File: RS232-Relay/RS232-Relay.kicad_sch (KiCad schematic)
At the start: 10 parts, among them J1 Conn_01x02, J2 Conn_01x02, K3 Relay_DPDT, Q1 2N3904, U2 4N25

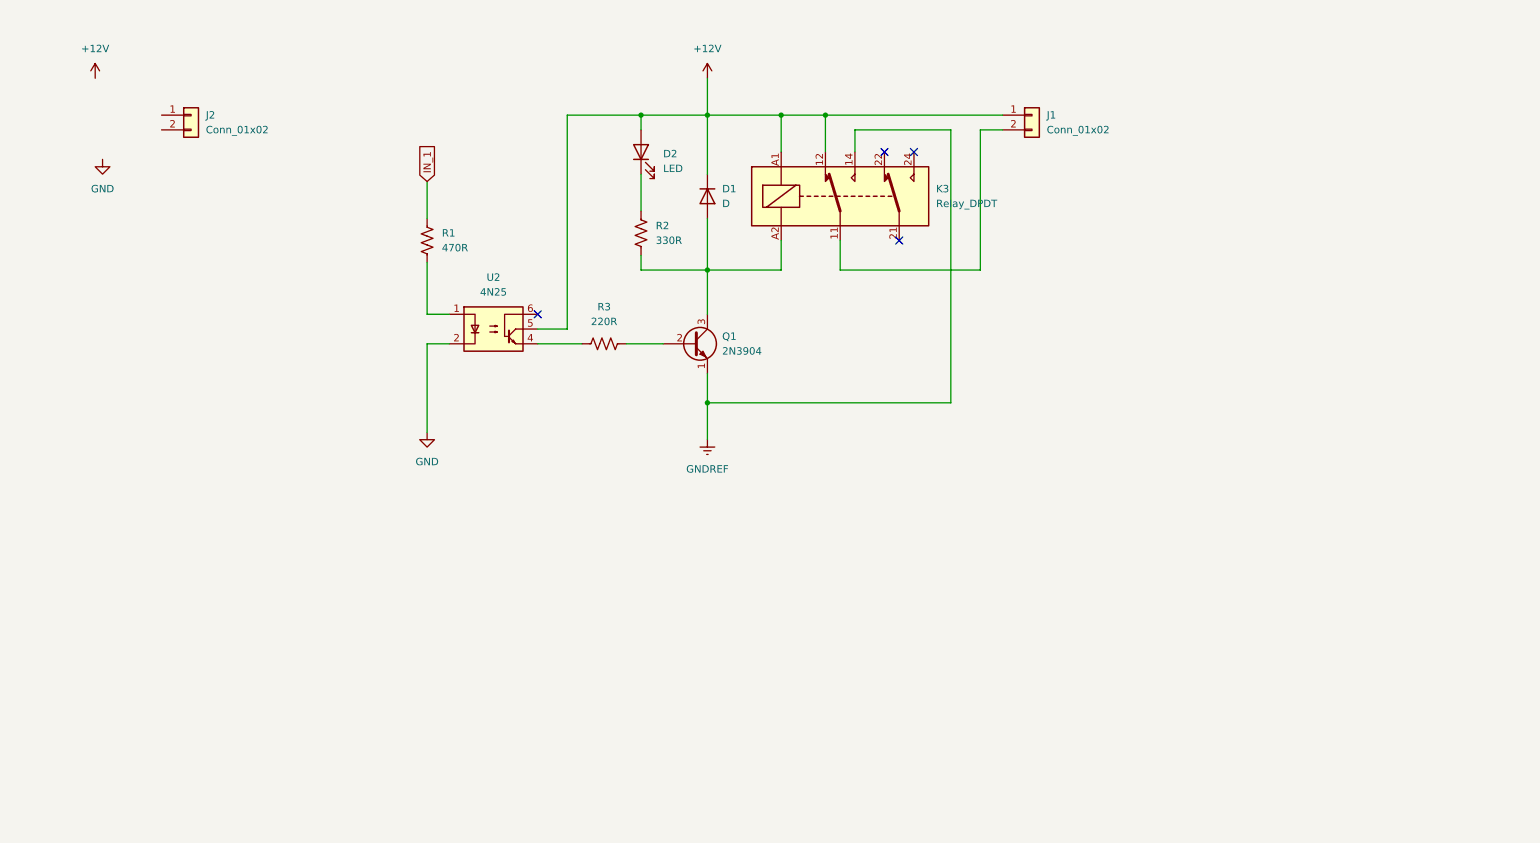
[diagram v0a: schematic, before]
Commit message: Relay layout
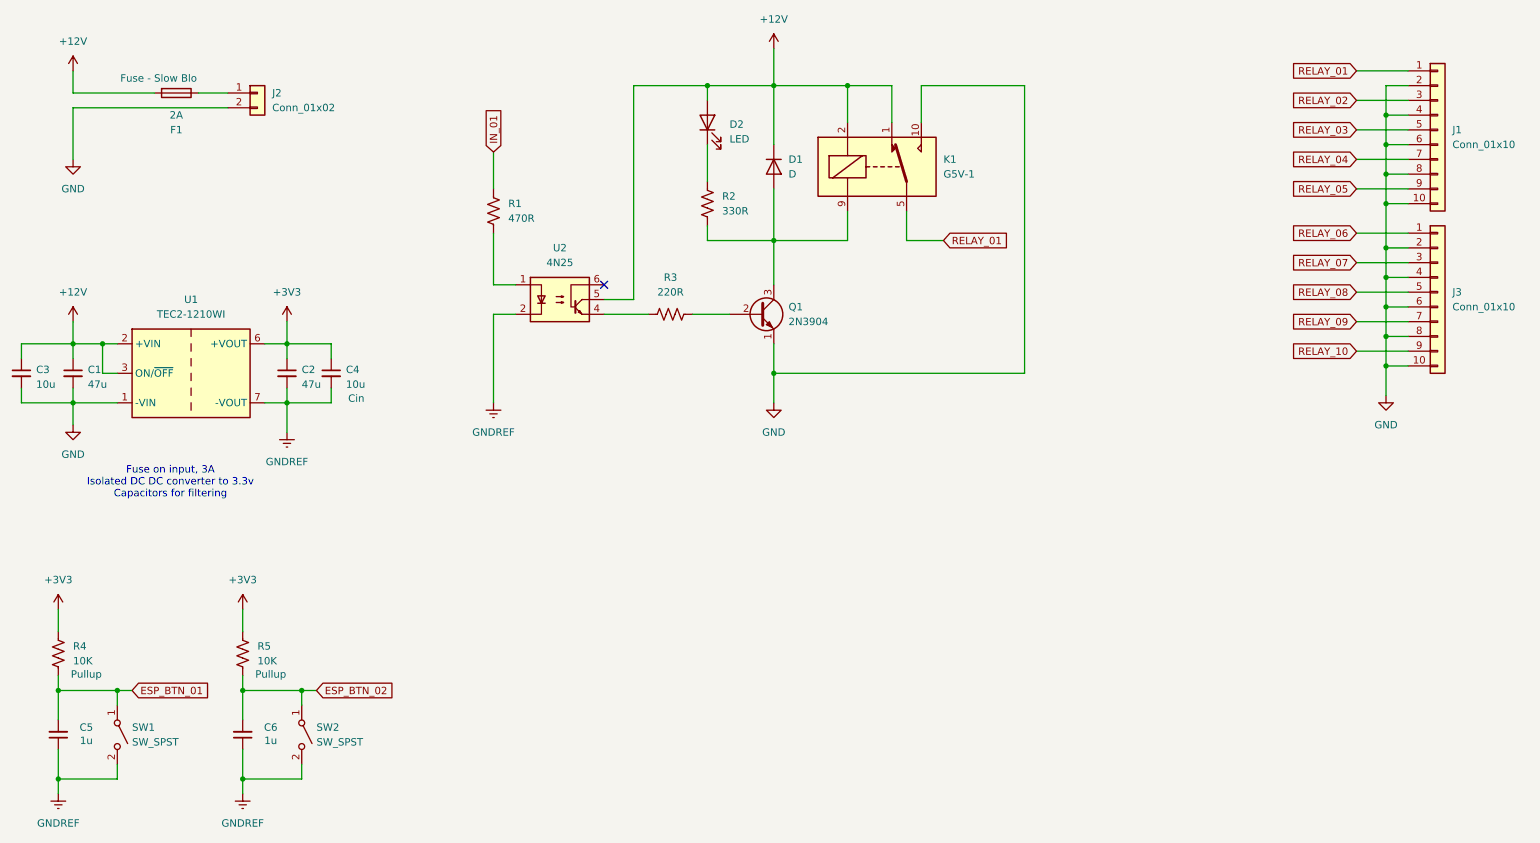
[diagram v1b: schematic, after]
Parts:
- removed J1: Conn_01x02, Connector_Phoenix_MSTB:PhoenixContact_MSTBA_2,5_2-G-5,08_1x02_P5.08mm_Horizontal, symbol Connector_Generic:Conn_01x02
- removed K3: Relay_DPDT, Relay_THT:Relay_DPDT_Omron_G5V-2, symbol Relay:Relay_DPDT
- added C1, C2: 47u, Capacitor_SMD:C_1206_3216Metric, symbol Device:C_Small
- added C3, C4: 10u, Capacitor_SMD:C_0603_1608Metric, symbol Device:C_Small
- added C5, C6: 1u, Capacitor_SMD:C_0402_1005Metric, symbol Device:C_Small
- added F1: 2A, Fuse:Fuseholder_Littelfuse_Nano2_154x, symbol Device:Fuse
- added J1, J3: Conn_01x10, Connector_Phoenix_MSTB:PhoenixContact_MSTBA_2,5_10-G-5,08_1x10_P5.08mm_Horizontal, symbol Connector_Generic:Conn_01x10
- added K1: G5V-1, Relay_THT:Relay_SPDT_Omron_G5V-1, symbol Relay:G5V-1
- added R4, R5: 10K, Resistor_SMD:R_0402_1005Metric, symbol Device:R_US
- added SW1, SW2: SW_SPST, Switch:PTS841, symbol Switch:SW_SPST
- added U1: TEC2-1210WI, Converter_DCDC:Converter_DCDC_TRACO_TMR-xxxx_THT, symbol Converter_DCDC:TEC2-1210WI
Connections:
- net +12V: now also C1.1, C3.1, F1.2, K1.1, K1.2, U1.2 (+VIN), U1.3 (ON/~{OFF})
- net GND: now also J2.2 (Pin_2), Q1.1 (E), C1.2, C3.2, J1.10 (Pin_10), J1.2 (Pin_2), J1.4 (Pin_4), J1.6 (Pin_6), J1.8 (Pin_8), J3.10 (Pin_10), J3.2 (Pin_2), J3.4 (Pin_4), J3.6 (Pin_6), J3.8 (Pin_8), K1.10, U1.1 (-VIN); no longer U2.2
- net GNDREF: now also U2.2, C2.2, C4.2, C5.1, C6.1, SW1.2 (B), SW2.2 (B), U1.7 (-VOUT); no longer Q1.1 (E)
- net at D1.2 (A), Q1.3 (C), R2.2: now also K1.9
- net at J2.1 (Pin_1): now also F1.1
- net IN_1 renamed IN_01
- new net +3V3: C2.1, C4.1, R4.1, R5.1, U1.6 (+VOUT)
- new net ESP_BTN_01: C5.2, R4.2, SW1.1 (A)
- new net ESP_BTN_02: C6.2, R5.2, SW2.1 (A)
- new net RELAY_01: J1.1 (Pin_1), K1.5, K1.6
- new net RELAY_02: J1.3 (Pin_3)
- new net RELAY_03: J1.5 (Pin_5)
- new net RELAY_04: J1.7 (Pin_7)
- new net RELAY_05: J1.9 (Pin_9)
- new net RELAY_06: J3.1 (Pin_1)
- new net RELAY_07: J3.3 (Pin_3)
- new net RELAY_08: J3.5 (Pin_5)
- new net RELAY_09: J3.7 (Pin_7)
- new net RELAY_10: J3.9 (Pin_9)
- no-connect marks 4 -> 1
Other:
- note added: "Fuse on input, 3A Isolated DC DC converter to 3.3v Capacitors for filtering"
- moved on the sheet: D1, D2, J2, Q1, R1, R2, R3, U2

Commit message: Including ESP32
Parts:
- removed C6: 1u, Capacitor_SMD:C_0402_1005Metric, symbol Device:C_Small
- removed R5: 10K, Resistor_SMD:R_0402_1005Metric, symbol Device:R_US
- removed SW2: SW_SPST, Switch:PTS841, symbol Switch:SW_SPST
- added J4, J5: Conn_01x09, symbol Connector_Generic:Conn_01x09
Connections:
- net +3V3: now also J4.3 (Pin_3)
- net GNDREF: now also J4.2 (Pin_2)
- new net +5V: J4.1 (Pin_1)
- new net ESP32_GPIO_14: J5.3 (Pin_3)
- new net ESP32_GPIO_15: J5.4 (Pin_4)
- new net ESP32_GPIO_18: J5.5 (Pin_5)
- new net ESP32_GPIO_19: J5.6 (Pin_6)
- new net ESP32_GPIO_20: J5.7 (Pin_7)
- new net ESP32_GPIO_21: J5.8 (Pin_8)
- new net ESP32_GPIO_22: J5.9 (Pin_9)
- new net ESP32_UART0_RX: J5.2 (Pin_2)
- new net ESP32_UART0_TX: J5.1 (Pin_1)
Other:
- note added: "3v3 input from ESP32"
- note removed: "Fuse on input, 3A Isolated DC DC converter to 3.3v Capacitors for filtering"

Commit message: Adding RS232
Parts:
- removed J1, J3: Conn_01x10, Connector_Phoenix_MSTB:PhoenixContact_MSTBA_2,5_10-G-5,08_1x10_P5.08mm_Horizontal, symbol Connector_Generic:Conn_01x10
- added J1, J3, J6: Conn_01x08, Connector_Phoenix_MSTB:PhoenixContact_MSTBA_2,5_8-G-5,08_1x08_P5.08mm_Horizontal, symbol Connector_Generic:Conn_01x08
- added J7: Conn_01x03, symbol Connector_Generic:Conn_01x03
- added R5: 220R, Resistor_SMD:R_0603_1608Metric, symbol Device:R_US
- added U3, U4: MAX3232, symbol Interface_UART:MAX3232
- J4, J5: footprint (none) -> Connector_PinHeader_2.54mm:PinHeader_1x09_P2.54mm_Vertical
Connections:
- net ESP32_GPIO_00: now also J4.4 (Pin_4)
- net ESP32_GPIO_01: now also J4.5 (Pin_5)
- net ESP32_GPIO_02: now also J4.6 (Pin_6)
- net ESP32_GPIO_03: now also J4.7 (Pin_7)
- net ESP32_GPIO_04: now also J4.8 (Pin_8)
- net ESP32_GPIO_05: now also J4.9 (Pin_9)
- net GND: now also J1.2 (Pin_2), J1.4 (Pin_4), J1.6 (Pin_6), J1.8 (Pin_8), J3.2 (Pin_2), J3.4 (Pin_4), J3.6 (Pin_6), J3.8 (Pin_8), J6.2 (Pin_2), J6.4 (Pin_4), J6.6 (Pin_6), J6.8 (Pin_8)
- net RELAY_01: now also J1.1 (Pin_1)
- net RELAY_02: now also J1.3 (Pin_3)
- net RELAY_03: now also J1.5 (Pin_5)
- net RELAY_04: now also J1.7 (Pin_7)
- net RELAY_05: now also J3.1 (Pin_1)
- net RELAY_06: now also J3.3 (Pin_3)
- net RELAY_07: now also J3.5 (Pin_5)
- net RELAY_08: now also J3.7 (Pin_7)
- net RELAY_09: now also J6.1 (Pin_1)
- net RELAY_10: now also J6.3 (Pin_3)
- new net RELAY_11: J6.5 (Pin_5)
- new net RELAY_12: J6.7 (Pin_7)
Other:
- note added: "12.5mA coil current"
- note added: "Calc this value"
- note added: "Check spacing of this to edge of board"
- note added: "Connect this to ESP32"
- note added: "Consider if capacitors are needed or left blank"
- note added: "Test points"

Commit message: Basic schematic fully complete
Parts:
- removed C3, C4: 10u, Capacitor_SMD:C_0603_1608Metric, symbol Device:C_Small
- removed C5: 1u, Capacitor_SMD:C_0402_1005Metric, symbol Device:C_Small
- removed SW1: SW_SPST, Switch:PTS841, symbol Switch:SW_SPST
- removed U3: MAX3232, symbol Interface_UART:MAX3232
- added C10, C11, C13, C6, C8, C9: 0.1uF, Capacitor_SMD:C_0402_1005Metric, symbol Device:C_Small
- added C12, C14, C15, C7: 1uF, Capacitor_SMD:C_0402_1005Metric, symbol Device:C_Small
- added D3, D4: WS2812B, LED_SMD:LED_WS2812B_PLCC4_5.0x5.0mm_P3.2mm, symbol LED:WS2812B
- added D5, D6, D7: Green, LED_SMD:LED_0805_2012Metric, symbol Device:LED
- added J8: RS232_2, Connector_Phoenix_MSTB:PhoenixContact_MSTBA_2,5_3-G-5,08_1x03_P5.08mm_Horizontal, symbol Connector_Generic:Conn_01x03
- added R10: 50R, Resistor_SMD:R_0603_1608Metric, symbol Device:R_US
- added R6, R7: 10K, Resistor_SMD:R_0402_1005Metric, symbol Device:R_US
- added R8: 4K7, Resistor_SMD:R_0603_1608Metric, symbol Device:R_US
- added R9: 220R, Resistor_SMD:R_0603_1608Metric, symbol Device:R_US
- added SW2, SW3: SW_SPST, Switch:PTS841, symbol Switch:SW_SPST
- added TP1: 3V3, TestPoint:TestPoint_Pad_D1.0mm, symbol Connector:TestPoint
- added TP10: I2C_SCL, TestPoint:TestPoint_Pad_D1.0mm, symbol Connector:TestPoint
- added TP11: I2C_INT, TestPoint:TestPoint_Pad_D1.0mm, symbol Connector:TestPoint
- added TP12: BTN_01, TestPoint:TestPoint_Pad_D1.0mm, symbol Connector:TestPoint
- added TP13: BTN_02, TestPoint:TestPoint_Pad_D1.0mm, symbol Connector:TestPoint
- added TP2: Signal In, TestPoint:TestPoint_Pad_D1.0mm, symbol Connector:TestPoint
- added TP3: Signal Out, TestPoint:TestPoint_Pad_D1.0mm, symbol Connector:TestPoint
- added TP4: GND_ISO, TestPoint:TestPoint_Pad_D1.0mm, symbol Connector:TestPoint
- added TP5: UART_1_TX, TestPoint:TestPoint_Pad_D1.0mm, symbol Connector:TestPoint
- added TP6: UART_1_RX, TestPoint:TestPoint_Pad_D1.0mm, symbol Connector:TestPoint
- added TP7: UART_2_TX, TestPoint:TestPoint_Pad_D1.0mm, symbol Connector:TestPoint
- added TP8: UART_2_RX, TestPoint:TestPoint_Pad_D1.0mm, symbol Connector:TestPoint
- added TP9: I2C_SDA, TestPoint:TestPoint_Pad_D1.0mm, symbol Connector:TestPoint
- added U3: PCF8575DBR, Package_SO:SSOP-24_5.3x8.2mm_P0.65mm, symbol Interface_Expansion:PCF8575DBR
- added U5: LTV-847S, Package_DIP:SMDIP-16_W9.53mm, symbol Isolator:LTV-847S
- C1, C2: value 47u -> 10u; footprint Capacitor_SMD:C_1206_3216Metric -> Capacitor_SMD:C_0603_1608Metric; LCSC C96123 -> C19702
- D1: value D -> 1N4148W
- D2: value LED -> RED
- F1: now not fitted; now left out of the parts list
- J1: value Conn_01x08 -> Relay 1-4
- J3: value Conn_01x08 -> Relay 5-8
- J6: value Conn_01x08 -> Relay 9-12
- J7: value Conn_01x03 -> RS232_1; footprint (none) -> Connector_Phoenix_MSTB:PhoenixContact_MSTBA_2,5_3-G-5,08_1x03_P5.08mm_Horizontal
- R1: value 470R -> 1000R; LCSC C23179 -> C21190
- R2: value 330R -> 1000R; LCSC C23138 -> C21190
- R4: value 10K -> 4K7; footprint Resistor_SMD:R_0402_1005Metric -> Resistor_SMD:R_0603_1608Metric; LCSC C25744 -> C23162
- U4: footprint (none) -> Package_SO:TSSOP-16_4.4x5mm_P0.65mm
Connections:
- net ESP_BTN_01 is gone; now on net +3V3: R4.2
- net IN_01 is gone; now on net +12V: R1.1
- net +12V: now also C2.1, J2.1 (Pin_1); no longer F1.2
- net +3V3: now also U4.16 (VCC), C12.2, C13.2, C7.2, C9.2, R10.2, R6.1, R7.1, R8.1, TP1.1, U3.24 (VCC); no longer C2.1, R4.1
- net +5V: now also D3.1 (VDD), D4.1 (VDD), R9.2
- net ESP32_GPIO_01: now also D3.4 (DIN)
- net ESP32_GPIO_03: now also R8.2, TP9.1, U3.23 (SDA)
- net ESP32_GPIO_04: now also R4.1, TP10.1, U3.22 (SCL)
- net ESP32_GPIO_05: now also TP11.1, U3.1 (~{INT})
- net ESP32_GPIO_14: now also U4.10 (T2IN), TP7.1
- net ESP32_GPIO_15: now also U4.9 (R2OUT), TP8.1
- net ESP32_UART0_RX: now also U4.12 (R1OUT), TP6.1
- net ESP32_UART0_TX: now also U4.11 (T1IN), TP5.1
- net GND: now also C2.2, D5.1 (K)
- net GNDREF: now also J7.3 (Pin_3), U4.15 (GND), C10.1, C11.1, C12.1, C13.1, C14.1, C15.1, C7.1, C9.1, D3.3 (VSS), D4.3 (VSS), D6.1 (K), D7.1 (K), J8.3 (Pin_3), SW2.2 (B), SW3.2 (B), TP4.1, U3.12 (GND), U3.2 (A1), U3.21 (A0), U3.3 (A2); no longer C2.2
- net RELAY_01: now also TP3.1
- net at R1.2: now also D5.2 (A); no longer U2.1
- net RS232_1_TX: now reaches J7.1 (Pin_1)
- net RS232_1_TX: now also U4.14 (T1OUT)
- net RS232_1_RX: now reaches J7.2 (Pin_2)
- net RS232_1_RX: now also U4.13 (R1IN)
- net at R5.1: now also U2.1
- net RELAY_IN_01: now reaches R5.2
- net RELAY_IN_01: now also TP2.1, U3.4 (P0)
- net at F1.1: no longer J2.1 (Pin_1)
- net at U4.1 (C1+): now also C6.1
- net at U4.2 (VS+): now also C11.2
- net at U4.3 (C1-): now also C6.2
- net at U4.4 (C2+): now also C8.2
- net at U4.5 (C2-): now also C8.1
- net at U4.6 (VS-): now also C10.2
- net RS232_2_TX: now reaches U4.7 (T2OUT)
- net RS232_2_TX: now also J8.1 (Pin_1)
- net RS232_2_RX: now reaches U4.8 (R2IN)
- net RS232_2_RX: now also J8.2 (Pin_2)
- net ESP32_GPIO_21 renamed BTN_01
- net BTN_01: now also C14.2, R6.2, SW2.1 (A), TP12.1
- net ESP32_GPIO_22 renamed BTN_02
- net BTN_02: now also C15.2, R7.2, SW3.1 (A), TP13.1
- new net: D3.2 (DOUT), D4.4 (DIN)
- new net: D6.2 (A), R10.1
- new net: D7.2 (A), R9.1
- new net RELAY_IN_02: U3.5 (P1)
- new net RELAY_IN_03: U3.6 (P2)
- new net RELAY_IN_04: U3.7 (P3)
- new net RELAY_IN_05: U3.8 (P4)
- new net RELAY_IN_06: U3.9 (P5)
- new net RELAY_IN_07: U3.10 (P6)
- new net RELAY_IN_08: U3.11 (P7)
- new net RELAY_IN_09: U3.13 (P10)
- new net RELAY_IN_10: U3.14 (P11)
- new net RELAY_IN_11: U3.15 (P12)
- new net RELAY_IN_12: U3.16 (P13)
- no-connect marks 1 -> 7
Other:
- note added: "10mA"
- note added: "12-3V DC-DC Regulator"
- note added: "12V power input"
- note added: "3.3v isolated from 12v using TEC2-1210WI"
- note added: "3v3 input from IO Expander (PCF8575DBR)"
- note added: "Buttons"
- note added: "How to calculate this value?"
- note added: "I2C Pullup"
- note added: "IO Expansion"
- note added: "If = 25mA (max) If = 10mA (target) Vf = 2V"
- note added: "If = 50mA (max) If = 10mA (target) Vf = 1.3V"
- note added: "Indicator LEDs"
- note added: "MIGRATE TO 5V regulator and use ESP32 onboard"
- note added: "RS232 Isolated Input Driver"
- note added: "Relay Outputs"
- note added: "Relay flips between 0 and 12V for output"
- note added: "Test Points"
- note removed: "3v3 input from ESP32"
- note removed: "Calc this value"
- note removed: "Connect this to ESP32"
- note removed: "Consider if capacitors are needed or left blank"
- note removed: "Test points"
- moved on the sheet: D1, D2, J1, J2, J3, J6, J7, K1, Q1, R3, U1, U2

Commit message: Fixing pin headers
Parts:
- removed D3, D4: WS2812B, LED_SMD:LED_WS2812B_PLCC4_5.0x5.0mm_P3.2mm, symbol LED:WS2812B
- J4, J5: footprint Connector_PinHeader_2.54mm:PinHeader_1x09_P2.54mm_Vertical -> Connector_PinSocket_2.54mm:PinSocket_1x09_P2.54mm_Vertical

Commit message: Schematic complete
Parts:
- removed D1: 1N4148W, Diode_SMD:D_SOD-123, symbol Device:D
- removed D2: RED, LED_SMD:LED_0805_2012Metric, symbol Device:LED
- removed K1: G5V-1, Relay_THT:Relay_SPDT_Omron_G5V-1, symbol Relay:G5V-1
- removed Q1: 2N3904, Package_TO_SOT_SMD:SOT-23, symbol Transistor_BJT:2N3904
- removed R2: 1000R, Resistor_SMD:R_0603_1608Metric, symbol Device:R_US
- removed R3, R5: 220R, Resistor_SMD:R_0603_1608Metric, symbol Device:R_US
- removed TP2: Signal In, TestPoint:TestPoint_Pad_D1.0mm, symbol Connector:TestPoint
- removed TP3: Signal Out, TestPoint:TestPoint_Pad_D1.0mm, symbol Connector:TestPoint
- removed U2: 4N25, Package_DIP:DIP-6_W7.62mm_SMDSocket_SmallPads, symbol Isolator:4N25
- removed U5: LTV-847S, Package_DIP:SMDIP-16_W9.53mm, symbol Isolator:LTV-847S
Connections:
- net ESP32_GPIO_00 renamed ESP_32_GPIO_00
- net ESP32_GPIO_01 renamed ESP_32_GPIO_01
- net ESP32_GPIO_02 renamed ESP_32_GPIO_02
- net ESP32_GPIO_03 renamed I2C_SDA
- net ESP32_GPIO_04 renamed I2C_SCL
- net ESP32_GPIO_05 renamed I2C_INT
- net ESP32_GPIO_14 renamed UART_2_TX
- net ESP32_GPIO_15 renamed UART_2_RX
- net ESP32_GPIO_18 renamed ESP_32_GPIO_18
- net ESP32_GPIO_19 renamed ESP_32_GPIO_19
- net ESP32_GPIO_20 renamed ESP_32_GPIO_20
- net ESP32_UART0_RX renamed UART_1_RX
- net ESP32_UART0_TX renamed UART_1_TX
- no-connect marks 7 -> 12
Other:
- added sheet Relay-Module (RelayModule.kicad_sch)
- added sheet Relay-Module1 (RelayModule.kicad_sch)
- added sheet Relay-Module2 (RelayModule.kicad_sch)
- note removed: "10mA"
- note removed: "12.5mA coil current"
- note removed: "3.3v isolated from 12v using TEC2-1210WI"
- note removed: "3v3 input from IO Expander (PCF8575DBR)"
- note removed: "How to calculate this value?"
- note removed: "If = 25mA (max) If = 10mA (target) Vf = 2V"
- note removed: "If = 50mA (max) If = 10mA (target) Vf = 1.3V"
- note removed: "MIGRATE TO 5V regulator and use ESP32 onboard"
- note removed: "Relay flips between 0 and 12V for output"
- moved on the sheet: J5
